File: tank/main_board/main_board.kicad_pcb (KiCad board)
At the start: 2 copper layers, 70.3 x 55.2 mm, 43 parts, among them J1 PowerIn, J10 Bump1, J11 Programming Header, J12 SigOut, J13 Encoder0, J14 Encoder1, J16 PowerOut, J2 M1, J20 PowerMotor, J3 M2, J4 LEDs, J5 M0, J6 Spk, J7 Hall2, J8 Hall1, J9 Bump0, Q1 2N3904, U1 L7805, U2 ATMEGA328P-PU, U3 SN74HC595, U4 TB6612FNG, U5 TB6612FNG, Y1 Crystal

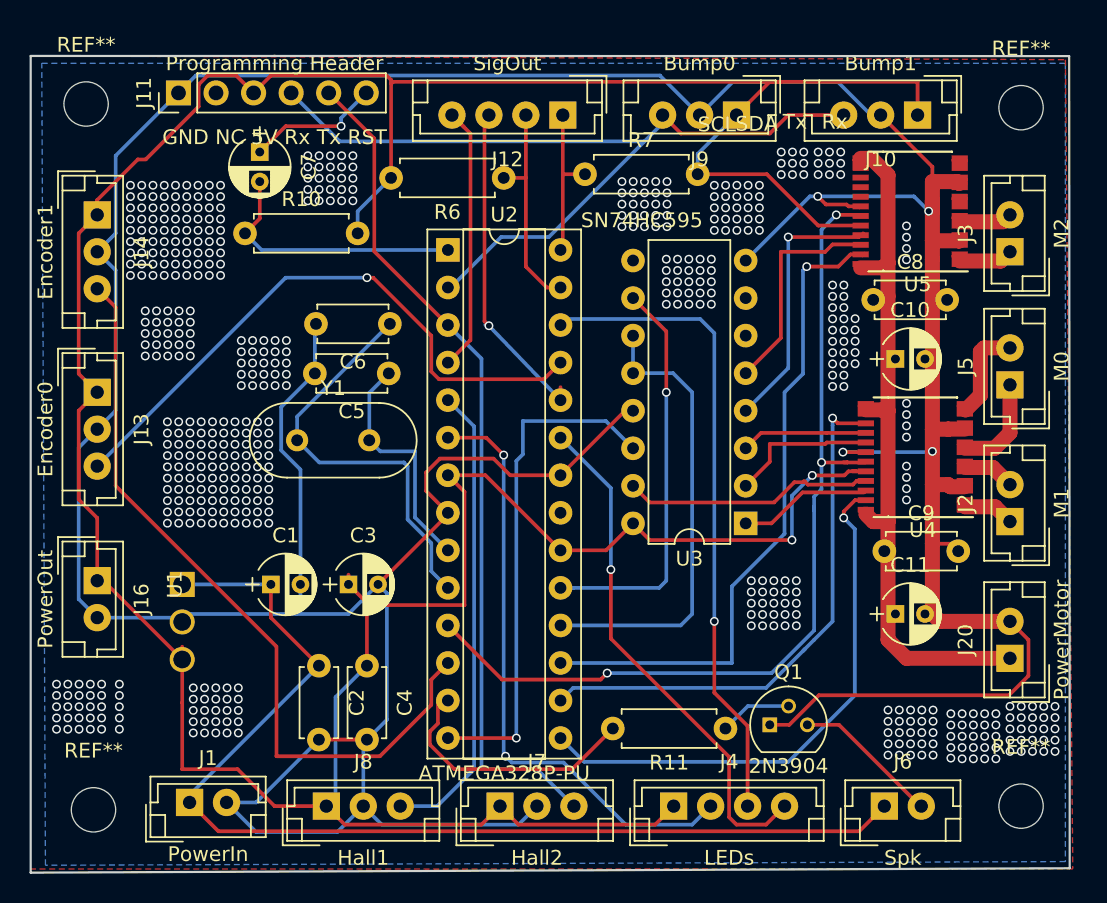
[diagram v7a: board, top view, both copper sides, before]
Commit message: Main Board Version 0.7
Had to switch around pins. Need M0 and M1 on the same PWM timer.
Need IR receiver pin to not interfere.
No point in ground traces with a ground plane.
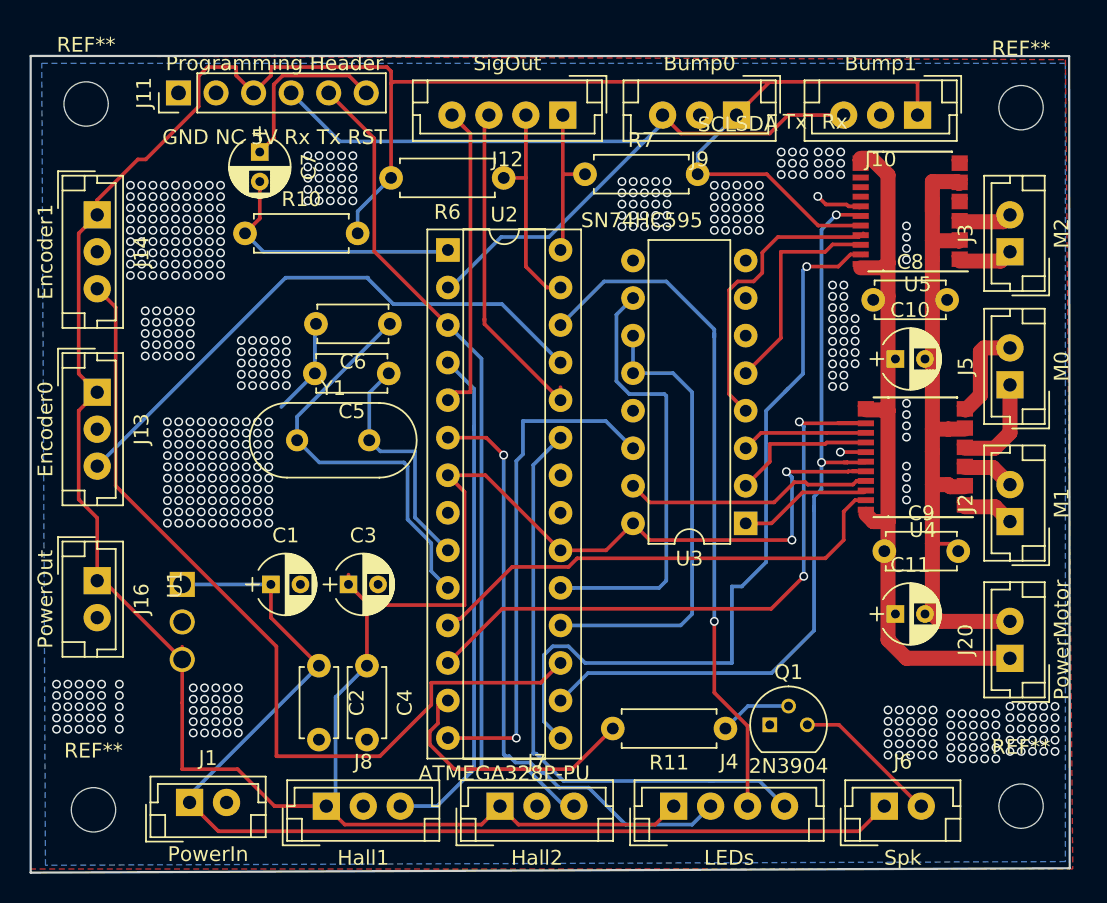
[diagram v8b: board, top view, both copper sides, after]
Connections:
- U2 pad 11: MEnable -> M0PWM
- U2 pad 12: Encoder1 -> M1PWM
- U2 pad 15: M0PWM -> M2PWM
- U2 pad 16: M1PWM -> MEnable
- U2 pad 17: M2PWM -> Encoder1
- U2 pad 4: IRRx -> TurretEncoder
- U2 pad 5: TurretEncoder -> IRRx
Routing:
- net GND: track 313.7 -> 64.3 mm, vias 520 -> 468
- net M2PWM: track 44.7 -> 53.3 mm
- net MEnable: track 61.6 -> 53.1 mm, vias 3 -> 2
- net Encoder1: track 51.9 -> 59.4 mm
- net M1PWM: track 36.9 -> 43.5 mm, vias 1 -> 2
- net LED2: track 34.9 -> 40.8 mm, vias 1 -> 0
- net 4.5V: track 245.6 -> 249.2 mm
- net M0PWM: track 37.0 -> 33.5 mm, vias 1 -> 0
- net IRRx: track 19.1 -> 22.2 mm
- net LED1: track 44.7 -> 47.8 mm
- net Net-(C7-Pad1): track 9.18 -> 12.0 mm, vias 1 -> 0
- net TurretEncoder: track 31.7 -> 34.5 mm
- net Encoder0: track 41.4 -> 39.1 mm, vias 1 -> 0
- net SRCLR: track 28.3 -> 30.6 mm, vias 1 -> 0
- net M2+: track 18.0 -> 20.0 mm, vias 1 -> 0
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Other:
- board text added: "Laser Tag Robot Tank Main Board v0.7 M.I.A.R. Labs nick.groesz@gmail.com"
- board text removed: "Laser Tag Robot Tank Main Board v0.6 M.I.A.R. Labs nick.groesz@gmail.com"
